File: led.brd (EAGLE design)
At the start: 13.6 x 12.7 mm, 3 parts

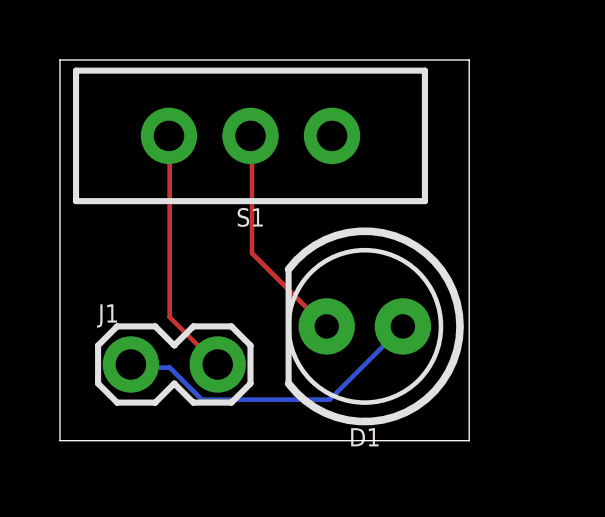
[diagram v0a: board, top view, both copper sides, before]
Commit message: Whoops! Forgot a resistor!
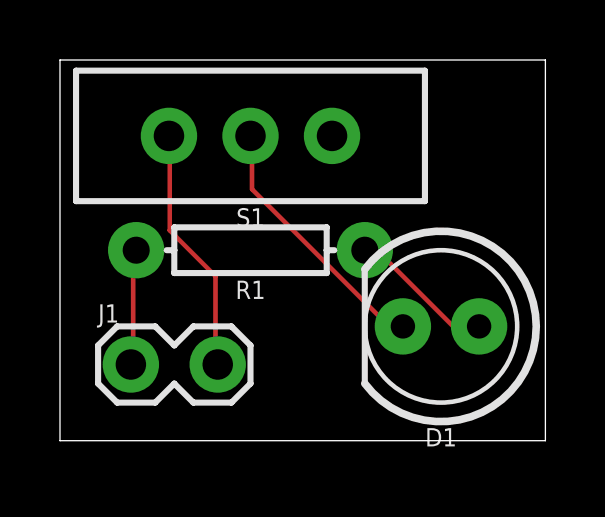
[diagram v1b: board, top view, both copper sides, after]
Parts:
- added R1: 220, SparkFun-Resistors:AXIAL-0.3
- moved D1 2.54 mm to (12.7, 3.81)
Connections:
- new net N$2: D1.A, R1.P$1
- net VCC: now also R1.P$2; no longer D1.A
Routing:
- net VCC: track 10.6 -> 4.02 mm
- net N$2: track 0.00 -> 4.88 mm
- net N$1: track 7.42 -> 8.71 mm
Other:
- board size 13.6 x 12.7 mm -> 16.2 x 12.7 mm
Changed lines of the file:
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@@
 <board>
 <plain>
-<wire x1="0" y1="0" x2="13.64" y2="0" width="0" layer="20"/>
-<wire x1="13.64" y1="0" x2="13.64" y2="12.69" width="0" layer="20"/>
-<wire x1="13.64" y1="12.69" x2="0" y2="12.69" width="0" layer="20"/>
+<wire x1="0" y1="0" x2="16.18" y2="0" width="0" layer="20"/>
+<wire x1="16.18" y1="0" x2="16.18" y2="12.69" width="0" layer="20"/>
+<wire x1="16.18" y1="12.69" x2="0" y2="12.69" width="0" layer="20"/>
 <wire x1="0" y1="12.69" x2="0" y2="0" width="0" layer="20"/>
 </plain>
@@
 </autorouter>
 <elements>
-<element name="D1" library="SparkFun-LED" package="LED_5MM" value="" x="10.16" y="3.81" smashed="yes" rot="R180">
-<attribute name="NAME" x="10.16" y="0.4191" size="0.6096" layer="25" font="vector" ratio="20" rot="R180" align="bottom-center"/>
-<attribute name="VALUE" x="10.1346" y="7.2009" size="0.6096" layer="27" font="vector" ratio="20" rot="R180" align="top-center"/>
+<element name="D1" library="SparkFun-LED" package="LED_5MM" value="" x="12.7" y="3.81" smashed="yes" rot="R180">
+<attribute name="NAME" x="12.7" y="0.4191" size="0.6096" layer="25" font="vector" ratio="20" rot="R180" align="bottom-center"/>
+<attribute name="VALUE" x="12.6746" y="7.2009" size="0.6096" layer="27" font="vector" ratio="20" rot="R180" align="top-center"/>
 </element>
 <element name="J1" library="SparkFun-Connectors" package="1X02_LOCK" value="" x="2.54" y="2.54" smashed="yes">
@@
 <attribute name="VALUE" x="6.35" y="12.573" size="0.6096" layer="27" font="vector" ratio="20" rot="R180" align="top-center"/>
 </element>
+<element name="R1" library="SparkFun-Resistors" package="AXIAL-0.3" value="220" x="6.35" y="6.35" smashed="yes" rot="R180">
+<attribute name="NAME" x="6.35" y="5.334" size="0.6096" layer="25" font="vector" ratio="20" rot="R180" align="bottom-center"/>
+<attribute name="PROD_ID" value=" " x="6.35" y="6.35" size="1.778" layer="27" rot="R180" display="off"/>
+<attribute name="VALUE" x="6.35" y="7.366" size="0.6096" layer="27" font="vector" ratio="20" rot="R180" align="top-center"/>
+</element>
 </elements>
 <signals>
@@
 <contactref element="S1" pad="1"/>
 <contactref element="J1" pad="2"/>
-<wire x1="3.6576" y1="4.1148" x2="3.6576" y2="10.0584" width="0.1524" layer="1"/>
-<wire x1="5.1816" y1="2.5908" x2="3.6576" y2="4.1148" width="0.1524" layer="1"/>
+<wire x1="3.6576" y1="7.0104" x2="3.6576" y2="10.0584" width="0.1524" layer="1"/>
+<wire x1="5.1816" y1="5.4864" x2="3.6576" y2="7.0104" width="0.1524" layer="1"/>
+<wire x1="5.1816" y1="2.5908" x2="5.1816" y2="5.4864" width="0.1524" layer="1"/>
 <wire x1="3.6576" y1="10.0584" x2="3.6322" y2="10.16" width="0.1524" layer="1"/>
 <wire x1="5.1816" y1="2.5908" x2="5.2578" y2="2.54" width="0.1524" layer="1"/>
@@
 <contactref element="S1" pad="2"/>
 <contactref element="D1" pad="K"/>
-<wire x1="6.4008" y1="6.2484" x2="6.4008" y2="10.0584" width="0.1524" layer="1"/>
-<wire x1="8.8392" y1="3.81" x2="6.4008" y2="6.2484" width="0.1524" layer="1"/>
+<wire x1="10.9728" y1="3.81" x2="11.43" y2="3.81" width="0.1524" layer="1"/>
+<wire x1="6.4008" y1="8.382" x2="10.9728" y2="3.81" width="0.1524" layer="1"/>
+<wire x1="6.4008" y1="10.0584" x2="6.4008" y2="8.382" width="0.1524" layer="1"/>
 <wire x1="6.4008" y1="10.0584" x2="6.35" y2="10.16" width="0.1524" layer="1"/>
-<wire x1="8.8392" y1="3.81" x2="8.89" y2="3.81" width="0.1524" layer="1"/>
 </signal>
 <signal name="VCC">
+<contactref element="J1" pad="1"/>
+<wire x1="2.4384" y1="2.4384" x2="2.3622" y2="2.54" width="0.1524" layer="16"/>
+<contactref element="R1" pad="P$2"/>
+<wire x1="2.4384" y1="6.2484" x2="2.4384" y2="2.5908" width="0.1524" layer="1"/>
+<wire x1="2.4384" y1="2.5908" x2="2.3622" y2="2.54" width="0.1524" layer="1"/>
+<wire x1="2.4384" y1="6.2484" x2="2.54" y2="6.35" width="0.1524" layer="1"/>
+</signal>
+<signal name="N$2">
 <contactref element="D1" pad="A"/>
-<contactref element="J1" pad="1"/>
-<wire x1="3.6576" y1="2.4384" x2="2.4384" y2="2.4384" width="0.1524" layer="16"/>
-<wire x1="4.7244" y1="1.3716" x2="3.6576" y2="2.4384" width="0.1524" layer="16"/>
-<wire x1="8.9916" y1="1.3716" x2="4.7244" y2="1.3716" width="0.1524" layer="16"/>
-<wire x1="11.43" y1="3.81" x2="8.9916" y2="1.3716" width="0.1524" layer="16"/>
-<wire x1="2.4384" y1="2.4384" x2="2.3622" y2="2.54" width="0.1524" layer="16"/>
+<contactref element="R1" pad="P$1"/>
+<wire x1="13.1064" y1="3.81" x2="13.97" y2="3.81" width="0.1524" layer="1"/>
+<wire x1="10.668" y1="6.2484" x2="13.1064" y2="3.81" width="0.1524" layer="1"/>
+<wire x1="10.2108" y1="6.2484" x2="10.668" y2="6.2484" width="0.1524" layer="1"/>
+<wire x1="10.2108" y1="6.2484" x2="10.16" y2="6.35" width="0.1524" layer="1"/>
 </signal>
 </signals>
